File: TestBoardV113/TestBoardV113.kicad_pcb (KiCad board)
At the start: 2 copper layers, 96 x 87.2 mm, 99 parts, among them J1 Conn_01x02_Socket, J10 Conn_01x02_Pin, J11 Conn_01x02_Pin, J12 Conn_01x02_Pin, J13 Conn_02x03_Odd_Even, J14 Conn_02x03_Odd_Even, J15 Conn_01x02_Pin, J16 Conn_02x03_Odd_Even, J17 Conn_01x01_Pin, J18 Conn_01x28_Socket, J19 Conn_01x01_Pin, J2 Conn_02x06_Odd_Even, J20 Conn_01x01_Pin, J21 Conn_01x28_Socket, J22 Conn_01x02_Pin, J23 Conn_01x02_Socket, J24 Conn_01x01_Pin, J25 Conn_01x02_Pin, J26 Conn_01x02_Pin, J27 Conn_02x03_Odd_Even, J28 Conn_01x02_Socket, J3 Conn_01x02_Pin, J4 Conn_01x02_Pin, J5 Conn_01x02_Pin, J6 Conn_01x02_Pin, J7 Conn_01x03_Pin, J8 Conn_01x03_Pin, J9 Conn_01x03_Pin, SW1 SW_DIP_x07, U3 NCP705MTADJTCG, U4 TAR5SxxU_SOT353F, U5 TXB0104PW, U6 TXB0104PW

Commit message: Changed some names
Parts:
- FC1_A+1, FC1_A-1, FC1_D+1, FC1_D-1, FC2_A+1, FC2_A-1, FC2_D+1, FC2_D-1, Vout1_NF1, Vout2_NF1, Vout_F1, Vout_Load1: value Testpoint -> TestPoint
- U1, U2: value ~ -> NCP705MTADJTCG
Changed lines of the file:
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@@
         (effects (font (size 1 1) (thickness 0.15)))
     )
-    (fp_text value "Testpoint" (at 0 2.25) (layer "F.Fab")
+    (fp_text value "TestPoint" (at 0 2.25) (layer "F.Fab")
         (effects (font (size 1 1) (thickness 0.15)))
     )
@@
         (effects (font (size 1 1) (thickness 0.15)))
     )
-    (fp_text value "Testpoint" (at 77.65 -26.48) (layer "F.Fab")
+    (fp_text value "TestPoint" (at 77.65 -26.48) (layer "F.Fab")
         (effects (font (size 1 1) (thickness 0.15)))
     )
@@
         (effects (font (size 1 1) (thickness 0.15)))
     )
-    (fp_text value "Testpoint" (at 77.65 -26.48) (layer "F.Fab")
+    (fp_text value "TestPoint" (at 77.65 -26.48) (layer "F.Fab")
         (effects (font (size 1 1) (thickness 0.15)))
     )
@@
         (effects (font (size 1 1) (thickness 0.15)))
     )
-    (fp_text value "Testpoint" (at 0 2.25) (layer "F.Fab")
+    (fp_text value "TestPoint" (at 0 2.25) (layer "F.Fab")
         (effects (font (size 1 1) (thickness 0.15)))
     )
@@
         (effects (font (size 1 1) (thickness 0.15)))
     )
-    (fp_text value "Testpoint" (at 0 2.25) (layer "F.Fab")
+    (fp_text value "TestPoint" (at 0 2.25) (layer "F.Fab")
         (effects (font (size 1 1) (thickness 0.15)))
     )
@@
         (effects (font (size 1 1) (thickness 0.15)))
     )
-    (fp_text value "Testpoint" (at 0 2.25) (layer "F.Fab")
+    (fp_text value "TestPoint" (at 0 2.25) (layer "F.Fab")
         (effects (font (size 1 1) (thickness 0.15)))
     )
@@
         (effects (font (size 1 1) (thickness 0.15)))
     )
-    (fp_text value "~" (at 0 1.95 90) (layer "F.Fab")
+    (fp_text value "NCP705MTADJTCG" (at 0 1.95 90) (layer "F.Fab")
         (effects (font (size 1 1) (thickness 0.15)))
     )
@@
         (effects (font (size 1 1) (thickness 0.15)))
     )
-    (fp_text value "Testpoint" (at 0 2.25) (layer "F.Fab")
+    (fp_text value "TestPoint" (at 0 2.25) (layer "F.Fab")
         (effects (font (size 1 1) (thickness 0.15)))
     )
@@
         (effects (font (size 1 1) (thickness 0.15)))
     )
-    (fp_text value "Testpoint" (at 0 2.25) (layer "F.Fab")
+    (fp_text value "TestPoint" (at 0 2.25) (layer "F.Fab")
         (effects (font (size 1 1) (thickness 0.15)))
     )
@@
         (effects (font (size 1 1) (thickness 0.15)))
     )
-    (fp_text value "Testpoint" (at 0 2.25) (layer "F.Fab")
+    (fp_text value "TestPoint" (at 0 2.25) (layer "F.Fab")
         (effects (font (size 1 1) (thickness 0.15)))
     )
@@
         (effects (font (size 1 1) (thickness 0.15)))
     )
-    (fp_text value "Testpoint" (at 0 2.25) (layer "F.Fab")
+    (fp_text value "TestPoint" (at 0 2.25) (layer "F.Fab")
         (effects (font (size 1 1) (thickness 0.15)))
     )
@@
         (effects (font (size 1 1) (thickness 0.15)))
     )
-    (fp_text value "Testpoint" (at 77.65 -26.48) (layer "F.Fab")
+    (fp_text value "TestPoint" (at 77.65 -26.48) (layer "F.Fab")
         (effects (font (size 1 1) (thickness 0.15)))
     )
@@
         (effects (font (size 1 1) (thickness 0.15)))
     )
-    (fp_text value "~" (at 0 1.95 90) (layer "F.Fab")
+    (fp_text value "NCP705MTADJTCG" (at 0 1.95 90) (layer "F.Fab")
         (effects (font (size 1 1) (thickness 0.15)))
     )
@@
         (effects (font (size 1 1) (thickness 0.15)))
     )
-    (fp_text value "Testpoint" (at 0 2.25 90) (layer "F.Fab")
+    (fp_text value "TestPoint" (at 0 2.25 90) (layer "F.Fab")
         (effects (font (size 1 1) (thickness 0.15)))
     )

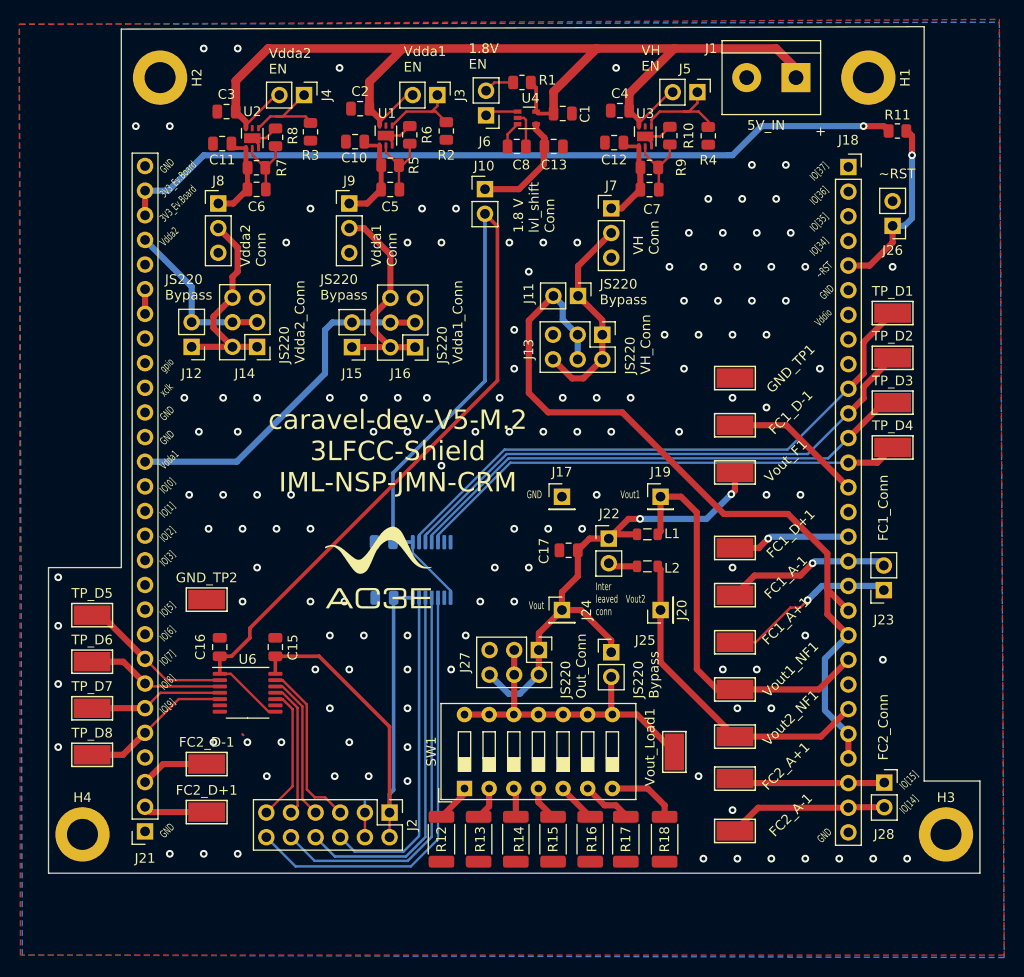
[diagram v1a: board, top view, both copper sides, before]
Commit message: added external load connector
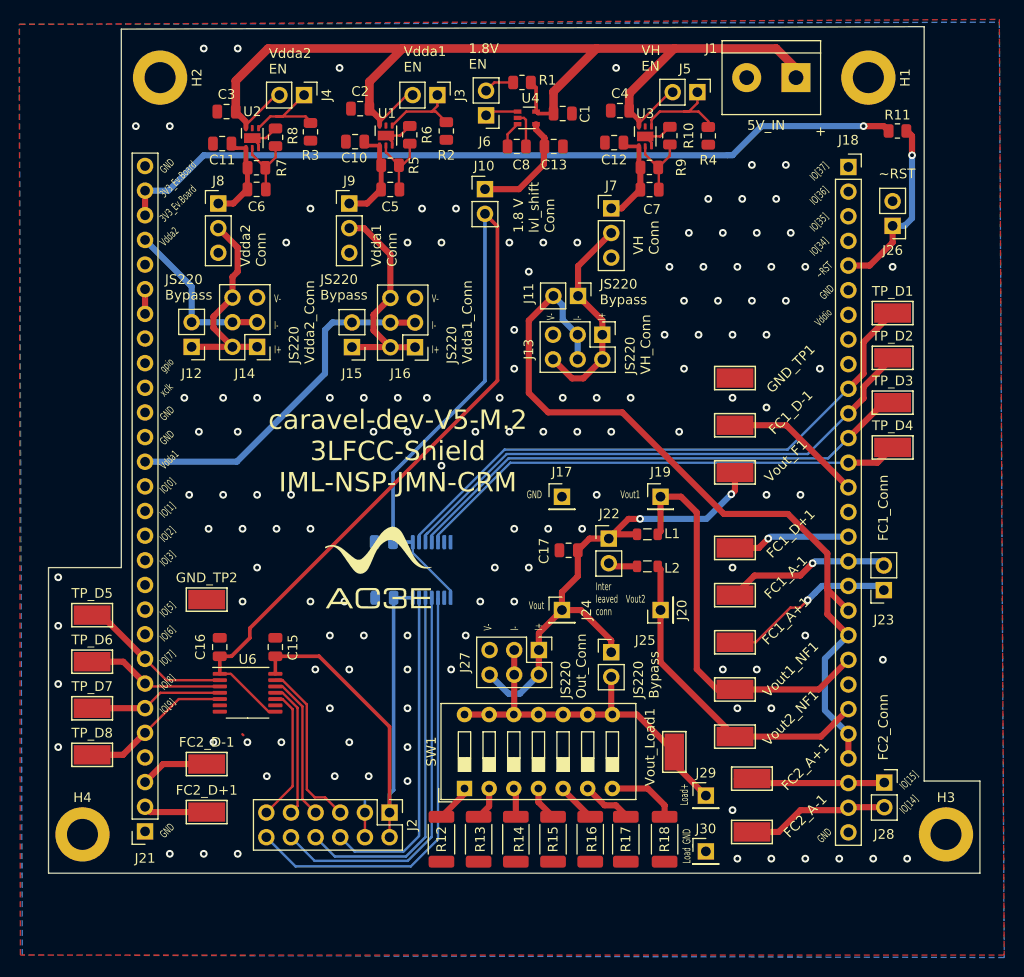
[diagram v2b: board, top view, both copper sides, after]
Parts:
- added J29: Conn_01x01_Pin, Connector_PinHeader_2.54mm:PinHeader_1x01_P2.54mm_Vertical, F.Cu at (163.8, 122.5)
- added J30: Conn_01x01_Pin, Connector_PinHeader_2.54mm:PinHeader_1x01_P2.54mm_Vertical, F.Cu at (163.8, 128.2)
- moved FC2_A-1 1.75 mm to (168.5, 126.2)
- moved FC2_A+1 1.75 mm to (168.5, 120.8)
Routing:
- net Load conection +: track 33.8 -> 39.7 mm
- net mprj_io[14]: track 16.4 -> 14.8 mm
- net mprj_io[15]: track 15.6 -> 14.5 mm
- net GND: vias 132 -> 130
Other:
- board text added: "I+"
- board text added: "I-"
- board text added: "Load+"
- board text added: "Load_GND"
- board text added: "V-"

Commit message: size cchanges
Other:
- board size 96 x 87.2 mm -> 96 x 86.8 mm
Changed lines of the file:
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@@
       (xy 192 121)
       (xy 186.25 121)
-      (xy 186.25 43.25)
-      (xy 103.5 43.5)
+      (xy 186 43.75)
+      (xy 103.5 43.75)
       (xy 103.5 99)
       (xy 96 99)
@@
   )
   (dimension (type aligned) (layer "Dwgs.User")
-    (pts (xy 186 130.5) (xy 186 44.5))
-    (height 41)
-    (gr_text "3385.8268 mils" (at 225.85 87.5 90) (layer "Dwgs.User")
+    (pts (xy 103.5 130.5) (xy 103.5 43.75))
+    (height -28)
+    (gr_text "86.7500 mm" (at 74.35 87.125 90) (layer "Dwgs.User")
       (effects (font (size 1 1) (thickness 0.15)))
     )
@@
   (dimension (type aligned) (layer "Dwgs.User")
     (pts (xy 96 130.5) (xy 192 130.5))
-    (height 20)
-    (gr_text "3779.5276 mils" (at 144 149.35) (layer "Dwgs.User")
+    (height 13)
+    (gr_text "96.0000 mm" (at 144 142.35) (layer "Dwgs.User")
       (effects (font (size 1 1) (thickness 0.15)))
     )
+    (format (prefix "") (suffix "") (units 3) (units_format 1) (precision 4))
+    (style (thickness 0.15) (arrow_length 1.27) (text_position_mode 0) (extension_height 0.58642) (extension_offset 0.5) keep_text_aligned)
+  )
+  (dimension (type aligned) (layer "Dwgs.User")
+    (pts (xy 186 43.75) (xy 186 130.5))
+    (height -11.25)
+    (gr_text "86.7500 mm" (at 196.1 87.125 90) (layer "Dwgs.User")
+      (effects (font (size 1 1) (thickness 0.15)))
+    )

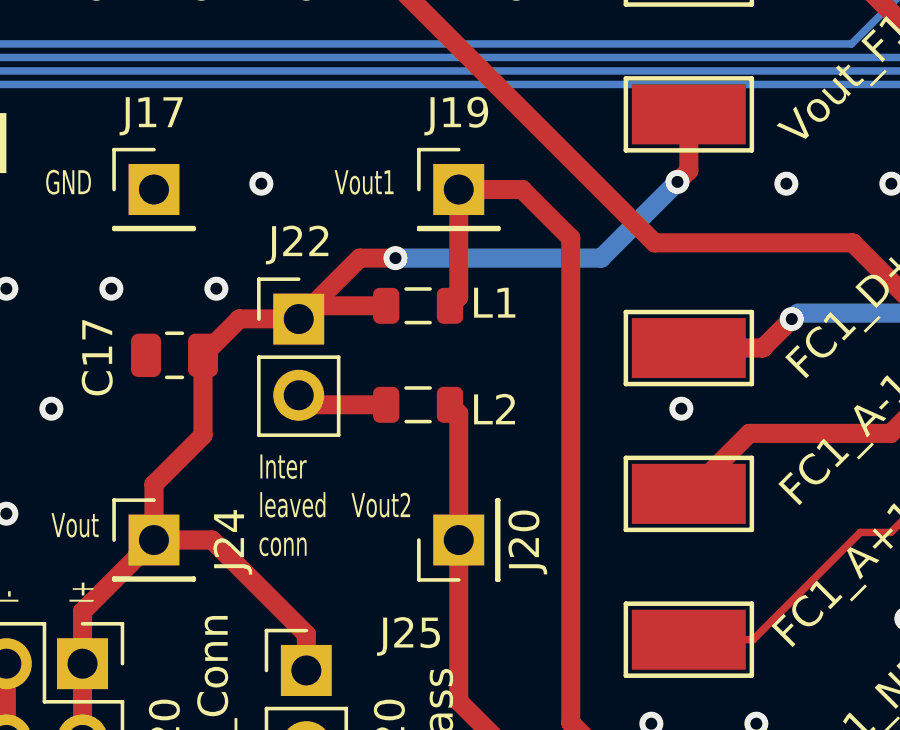
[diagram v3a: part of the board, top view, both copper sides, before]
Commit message: inductors size changed
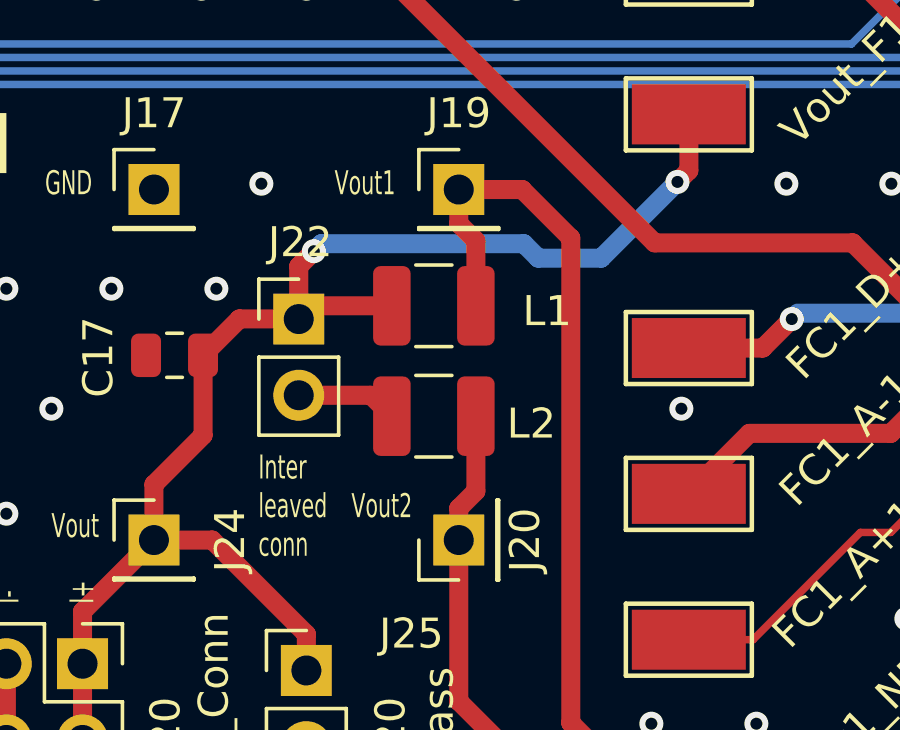
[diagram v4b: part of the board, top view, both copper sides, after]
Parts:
- L1, L2: footprint Inductor_SMD:L_0805_2012Metric -> Inductor_SMD:L_1210_3225Metric
- moved L2 0.65 mm to (158.2, 99.2)
- moved L1 0.53 mm to (158.2, 95.6)
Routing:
- net Net-(J22-Pin_1): track 52.5 -> 54.6 mm
- net Net-(J22-Pin_2): track 3.13 -> 3.85 mm
